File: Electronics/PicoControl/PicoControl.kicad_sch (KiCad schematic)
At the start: 15 parts, among them J1 Conn_01x03_Pin, J2 Conn_01x03_Socket, J4 Conn_01x06_Pin, U3 RX8025T-UB, U4 Pico

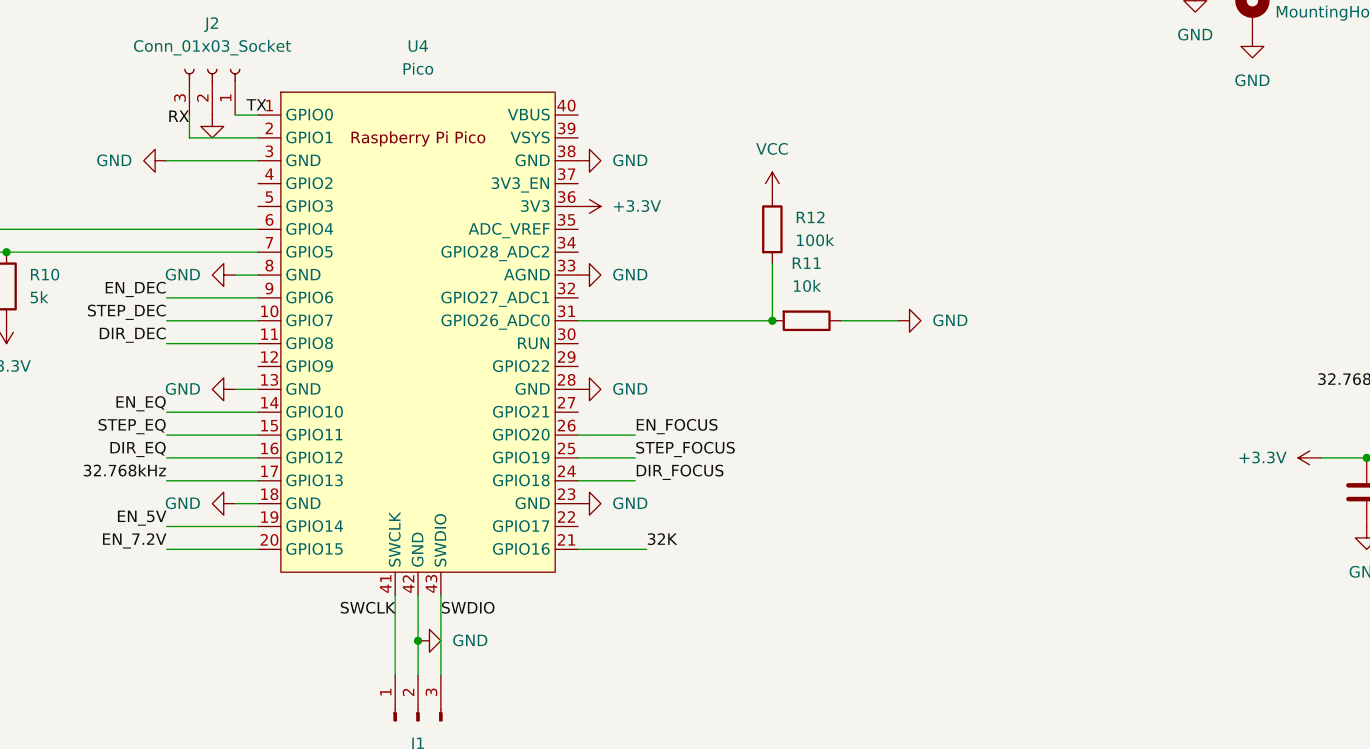
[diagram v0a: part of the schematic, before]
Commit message: Updated PCB to Include Hall Sensors
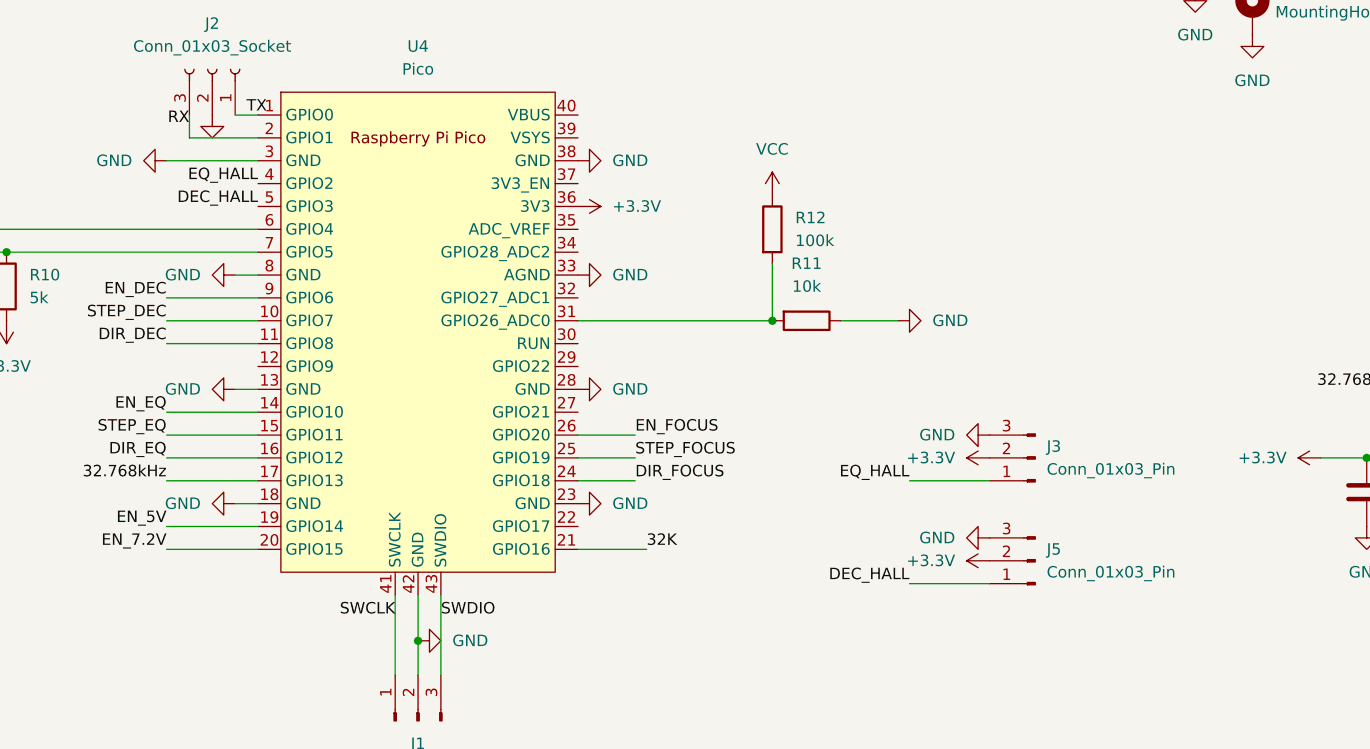
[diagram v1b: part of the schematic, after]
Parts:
- added J3, J5: Conn_01x03_Pin, Connector_PinHeader_2.54mm:PinHeader_1x03_P2.54mm_Horizontal, symbol Connector:Conn_01x03_Pin
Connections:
- net +3.3V: now also J3.2 (Pin_2), J5.2 (Pin_2)
- net GND: now also J3.3 (Pin_3), J5.3 (Pin_3)
- net EQ_HALL: now reaches U4.4 (GPIO2)
- net EQ_HALL: now also J3.1 (Pin_1)
- net DEC_HALL: now reaches U4.5 (GPIO3)
- net DEC_HALL: now also J5.1 (Pin_1)
